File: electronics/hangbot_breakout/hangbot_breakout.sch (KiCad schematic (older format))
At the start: 14 parts, among them J1 CONN_02X10, J10 CONN_01X02, J11 CONN_01X02, J2 CONN_01X04, J3 CONN_01X02, J4 CONN_01X02, J5 CONN_01X02, J6 CONN_01X02, J7 CONN_01X02, J8 CONN_01X02, J9 CONN_01X02

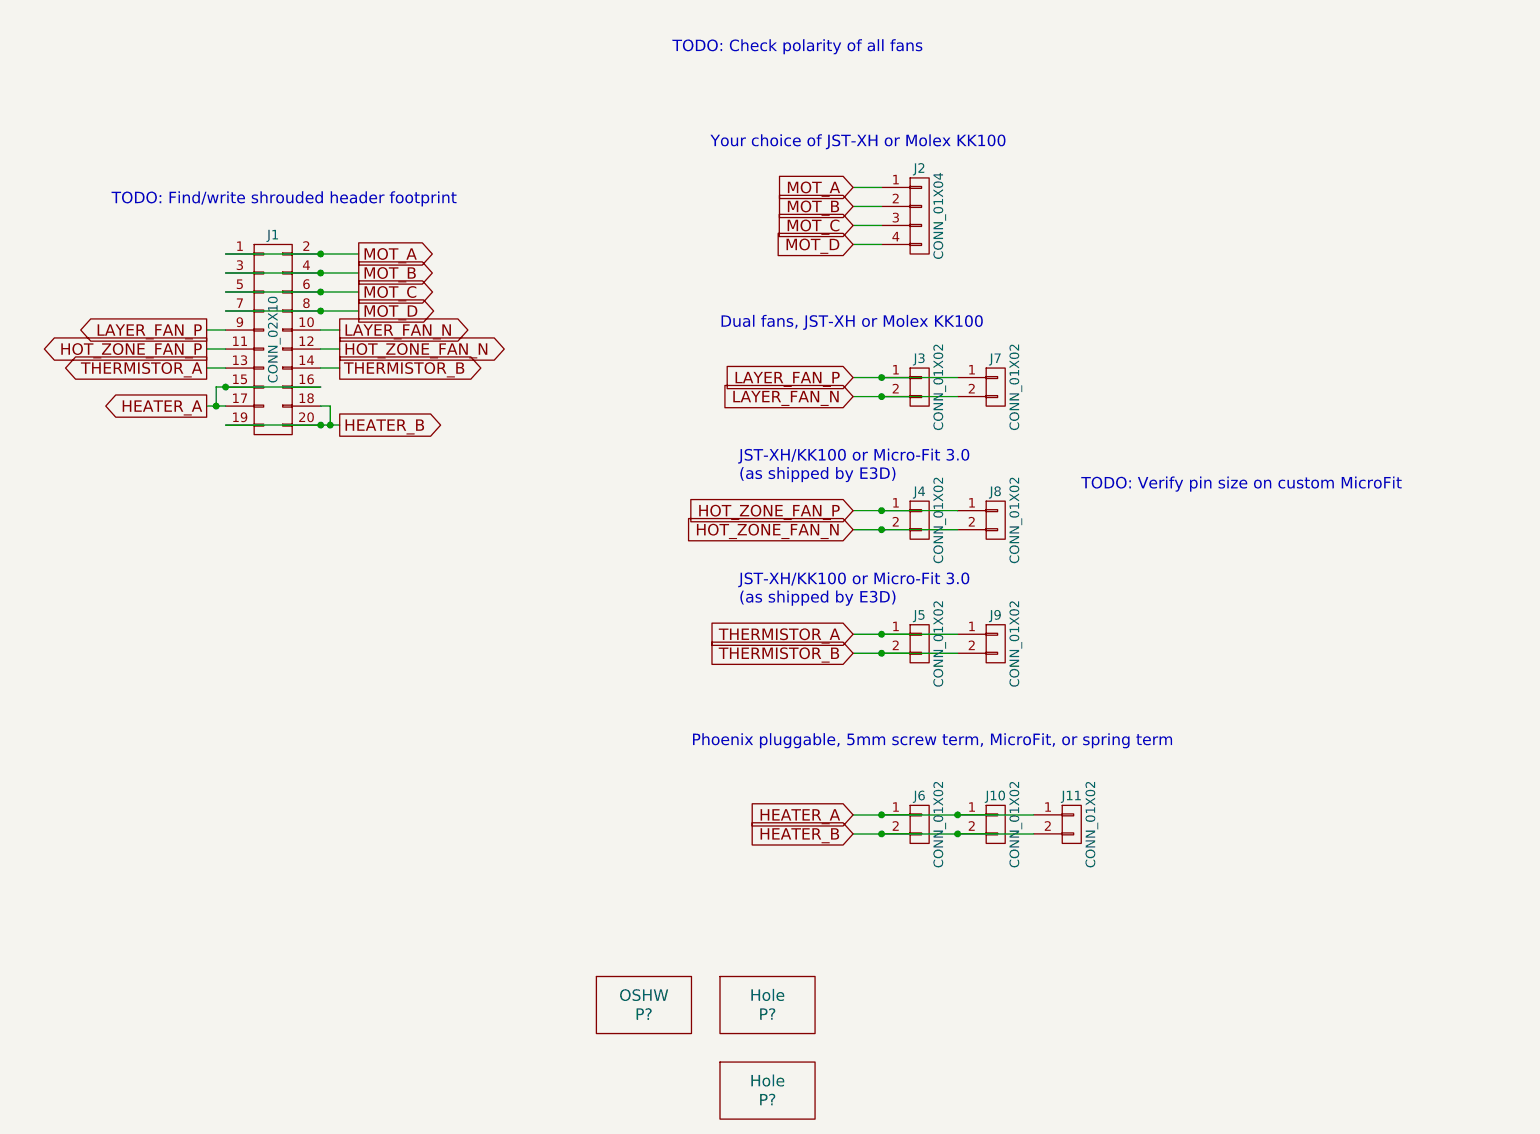
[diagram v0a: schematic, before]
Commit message: Re-layout board to be NEMA-17 sized.
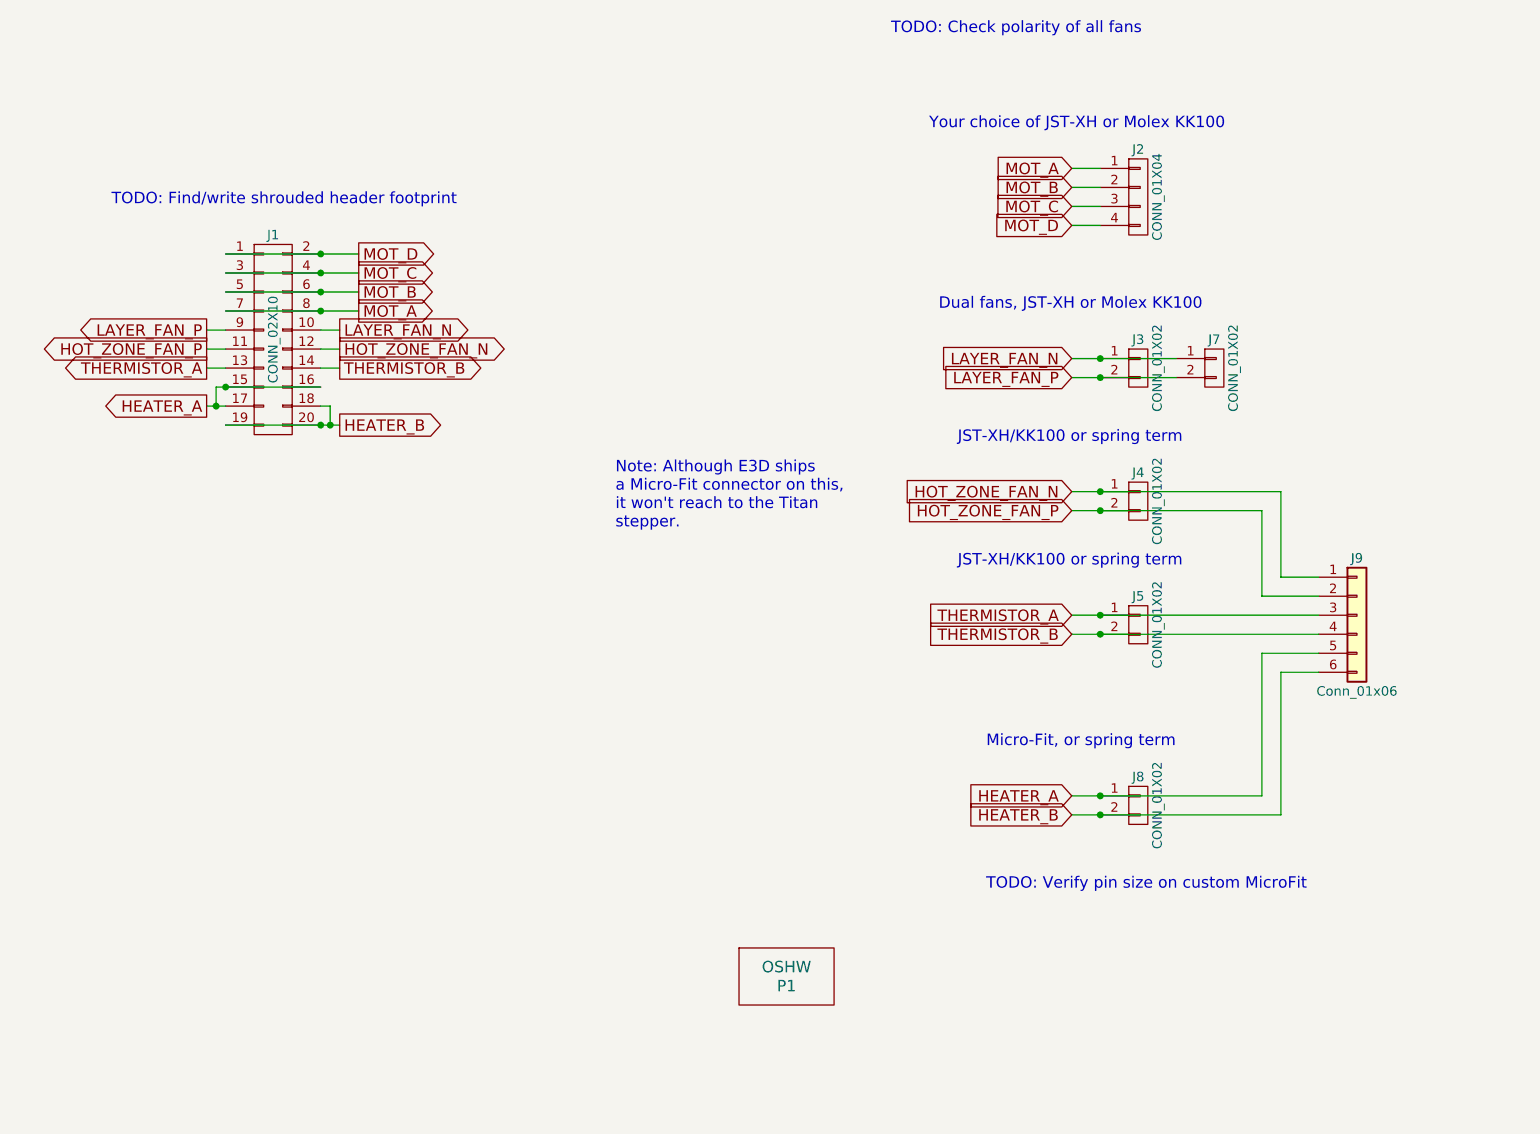
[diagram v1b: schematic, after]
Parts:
- removed J11: CONN_01X02, TerminalBlocks_KF235:KF235_2Pin_3.81mm, symbol CONN_01X02
- removed J6: CONN_01X02, Connectors_Phoenix:PhoenixContact_MSTBA-G_02x5.08mm_Angled, symbol CONN_01X02
- removed J8, J9: CONN_01X02, Connectors_Molex_MicroFit:Molex_MicroFit_43650-0200_2Pin, symbol CONN_01X02
- removed P? (x2): Hole, Mounting_Holes:MountingHole_3.2mm_M3_Pad_Via, symbol SYMBOL
- added J9: Conn_01x06, TerminalBlocks_TE:Spring_Horizontal_3.81mm_1-2834017-6, symbol Conn_01x06
- gave numbers to parts that had none: 1
- renumbered J10 to J8
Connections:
- net HEATER_A: now also J9.5 (Pin_5)
- net HEATER_B: now also J9.6 (Pin_6)
- net HOT_ZONE_FAN_N: now also J4.1 (P1), J9.1 (Pin_1); no longer J4.2 (P2)
- net HOT_ZONE_FAN_P: now also J4.2 (P2), J9.2 (Pin_2); no longer J4.1 (P1)
- net LAYER_FAN_N: now also J3.1 (P1), J7.1 (P1); no longer J3.2 (P2), J7.2 (P2)
- net LAYER_FAN_P: now also J3.2 (P2), J7.2 (P2); no longer J3.1 (P1), J7.1 (P1)
- net MOT_A: now also J1.7 (P7), J1.8 (P8); no longer J1.1 (P1), J1.2 (P2)
- net MOT_B: now also J1.5 (P5), J1.6 (P6); no longer J1.3 (P3), J1.4 (P4)
- net MOT_C: now also J1.3 (P3), J1.4 (P4); no longer J1.5 (P5), J1.6 (P6)
- net MOT_D: now also J1.1 (P1), J1.2 (P2); no longer J1.7 (P7), J1.8 (P8)
- net THERMISTOR_A: now also J9.3 (Pin_3)
- net THERMISTOR_B: now also J9.4 (Pin_4)
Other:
- note added: "JST-XH/KK100 or spring term"
- note added: "Micro-Fit, or spring term"
- note added: "Note: Although E3D ships\na Micro-Fit connector on this,\nit won't reach to the Titan\nstepper."
- note removed: "JST-XH/KK100 or Micro-Fit 3.0\n(as shipped by E3D)"
- note removed: "Phoenix pluggable, 5mm screw term, MicroFit, or spring term"
- moved on the sheet: J2, J3, J4, J5, J8, P1
